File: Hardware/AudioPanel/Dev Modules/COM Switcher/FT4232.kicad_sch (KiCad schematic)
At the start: 83 parts, among them J601 PC1_COM, J602 PC2_COM, J603 PC3_COM, J604 PC4_COM, J605 2.54mm, Q601 BCM857BS, U601 FT4232H, U602 93LCxxA, Y601 12MHz

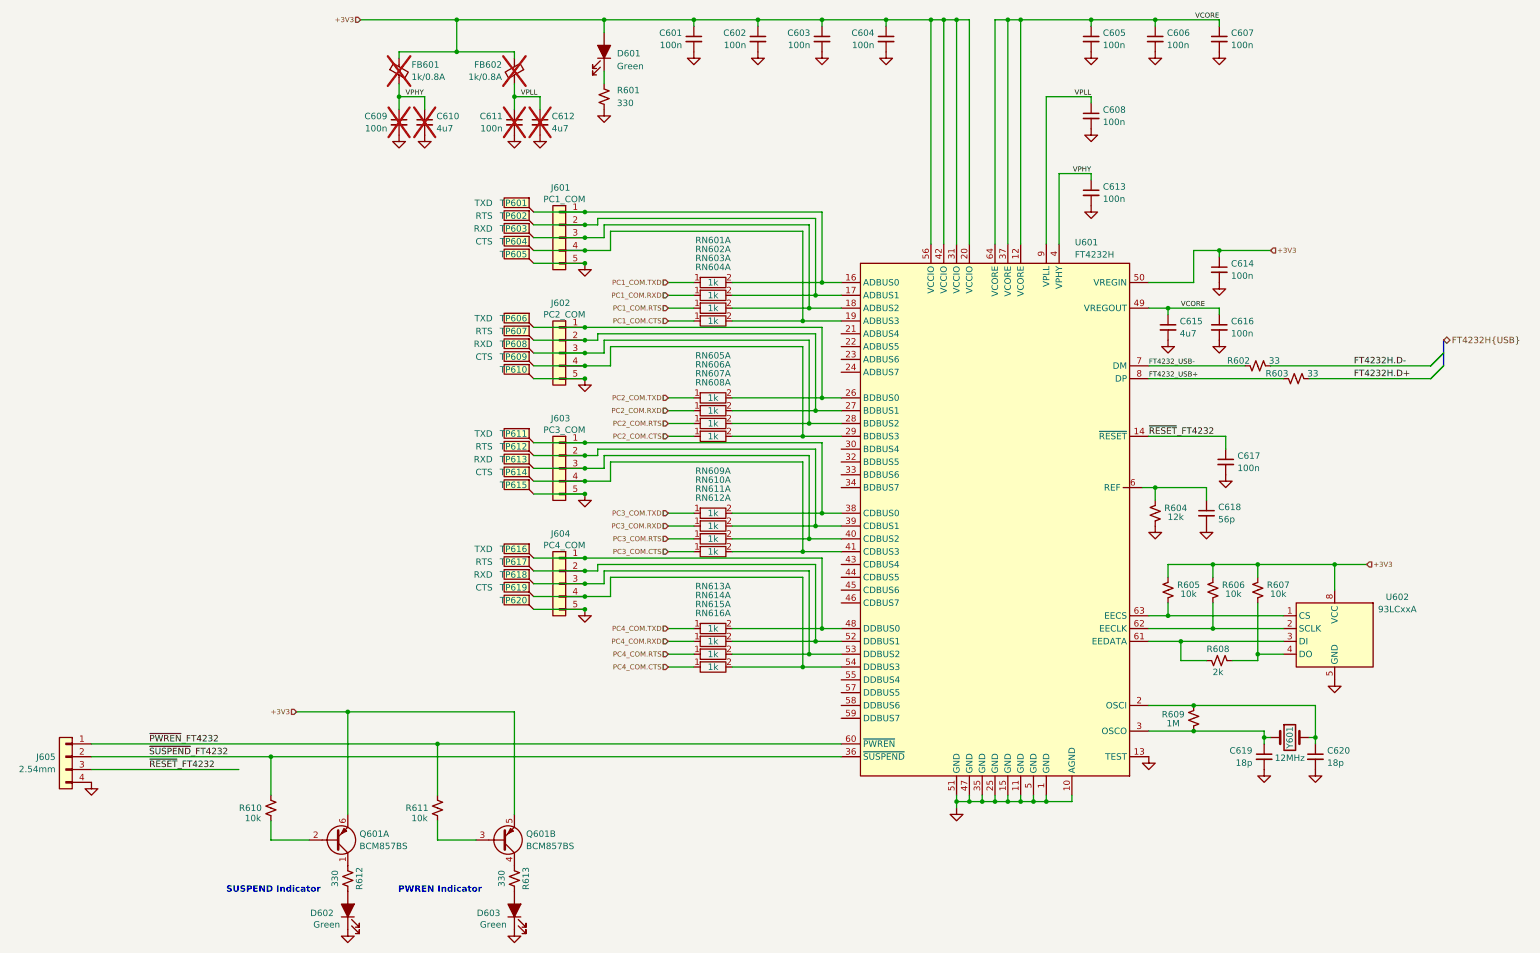
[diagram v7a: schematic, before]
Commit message: Fixed footprint errors, placed onto PCBs
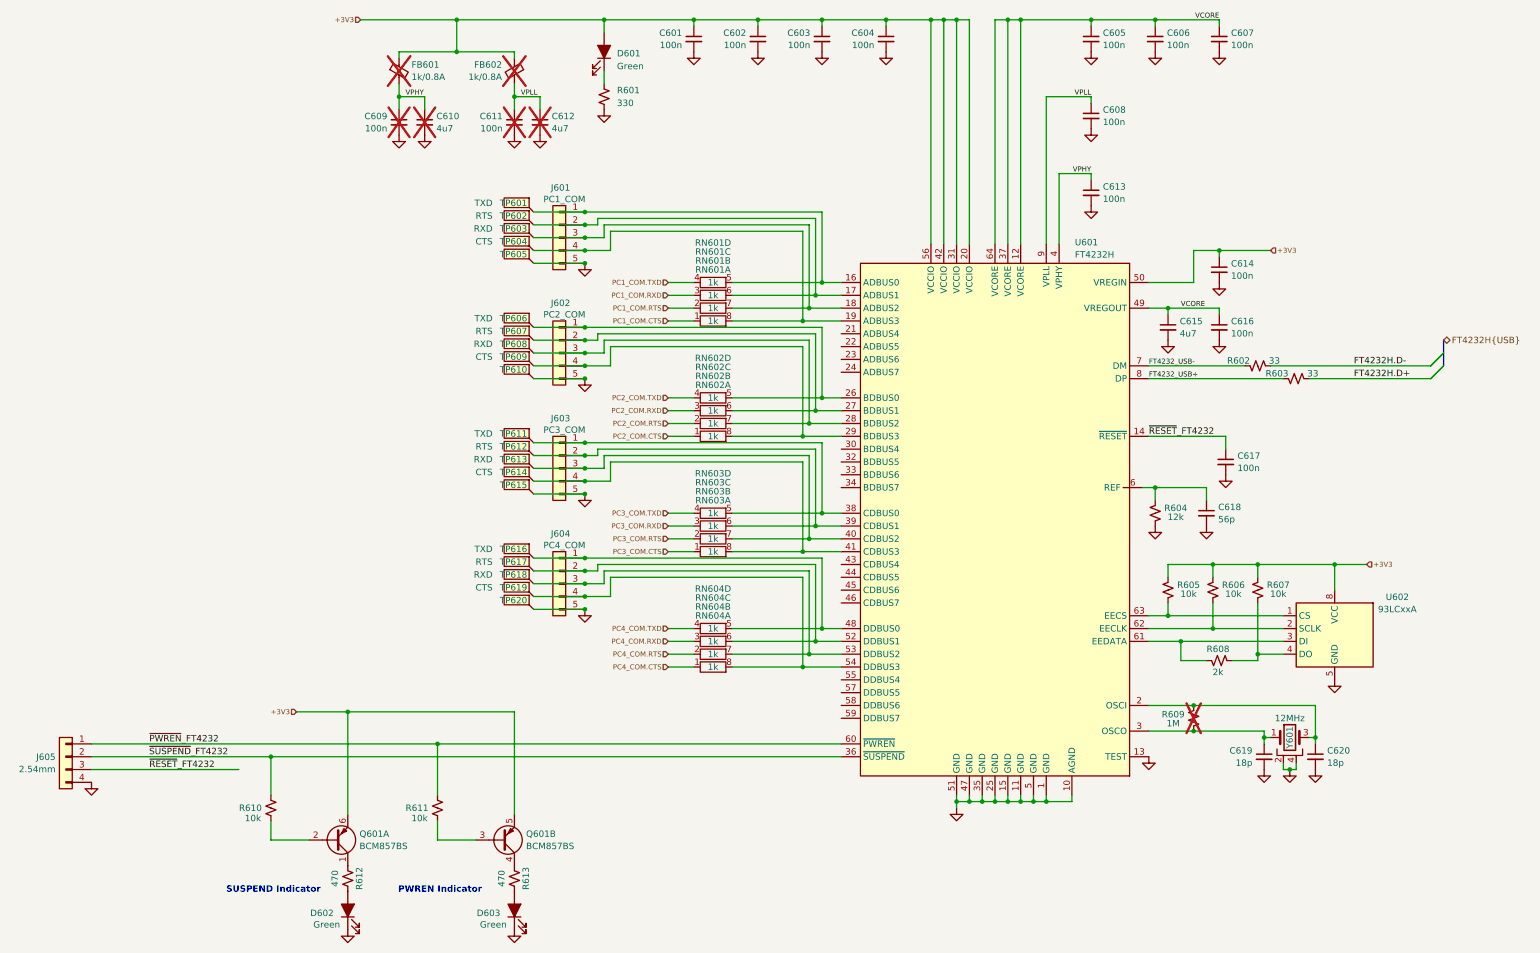
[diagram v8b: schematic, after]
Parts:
- removed RN605, RN606, RN607, RN608, RN609, RN610, RN611, RN612, RN613, RN614, RN615, RN616: 1k, Resistor_SMD:R_Array_Convex_4x1206, symbol Library_MicSwitcher:R_Network04_Split
- added unit 2 of RN601
- added unit 4 of RN601
- added unit 3 of RN601
- added unit 2 of RN602
- added unit 4 of RN602
- added unit 3 of RN602
- added unit 4 of RN603
- added unit 3 of RN603
- added unit 2 of RN603
- added unit 4 of RN604
- added unit 2 of RN604
- added unit 3 of RN604
- R609: now not fitted
- R612, R613: value 330 -> 470
- U601: footprint Package_DFN_QFN:QFN-56-1EP_8x8mm_P0.5mm_EP5.6x5.6mm -> Package_DFN_QFN:QFN-64-1EP_9x9mm_P0.5mm_EP6x6mm
- U602: footprint Package_SO:SOIC-8-1EP_3.9x4.9mm_P1.27mm_EP2.29x3mm -> Package_SO:SOIC-8_3.9x4.9mm_P1.27mm
- Y601: symbol Device:Crystal -> Device:Crystal_GND2
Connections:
- net GND: now also U601.65 (GND), Y601.2, Y601.4
- net PC1_COM.CTS: now also RN601.1 (4); no longer RN604.1
- net PC1_COM.RTS: now also RN601.2; no longer RN603.1
- net PC1_COM.RXD: now also RN601.3; no longer RN602.1
- net PC1_COM.TXD: now also RN601.4; no longer RN601.1
- net PC2_COM.CTS: now also RN602.1 (4)
- net PC2_COM.RTS: now also RN602.2
- net PC2_COM.RXD: now also RN602.3
- net PC2_COM.TXD: now also RN602.4
- net PC3_COM.CTS: now also RN603.1 (4)
- net PC3_COM.RTS: now also RN603.2
- net PC3_COM.RXD: now also RN603.3
- net PC3_COM.TXD: now also RN603.4
- net PC4_COM.CTS: now also RN604.1 (4)
- net PC4_COM.RTS: now also RN604.2
- net PC4_COM.RXD: now also RN604.3
- net PC4_COM.TXD: now also RN604.4
- net at J603.4 (Pin_4), TP614.1, U601.41 (CDBUS3): now also RN603.8
- net at J603.3 (Pin_3), TP613.1, U601.40 (CDBUS2): now also RN603.7 (5)
- net at J604.3 (Pin_3), TP618.1, U601.53 (DDBUS2): now also RN604.7 (5)
- net at J601.3 (Pin_3), TP603.1, U601.18 (ADBUS2): now also RN601.7 (5); no longer RN603.2
- net at J602.3 (Pin_3), TP608.1, U601.28 (BDBUS2): now also RN602.7 (5)
- net at J603.2 (Pin_2), TP612.1, U601.39 (CDBUS1): now also RN603.6
- net at J602.1 (Pin_1), TP606.1, U601.26 (BDBUS0): now also RN602.5
- net at J604.1 (Pin_1), TP616.1, U601.48 (DDBUS0): now also RN604.5
- net at J604.2 (Pin_2), TP617.1, U601.52 (DDBUS1): now also RN604.6
- net at J604.4 (Pin_4), TP619.1, U601.54 (DDBUS3): now also RN604.8
- net at C620.1, R609.2, U601.2 (OSCI): now also Y601.3; no longer Y601.2
- net at J601.4 (Pin_4), TP604.1, U601.19 (ADBUS3): now also RN601.8; no longer RN604.2
- net at J602.4 (Pin_4), TP609.1, U601.29 (BDBUS3): now also RN602.8
- net at J603.1 (Pin_1), TP611.1, U601.38 (CDBUS0): now also RN603.5
- net at J602.2 (Pin_2), TP607.1, U601.27 (BDBUS1): now also RN602.6
- net at J601.1 (Pin_1), TP601.1, U601.16 (ADBUS0): now also RN601.5; no longer RN601.2
- net at J601.2 (Pin_2), TP602.1, U601.17 (ADBUS1): now also RN601.6; no longer RN602.2
